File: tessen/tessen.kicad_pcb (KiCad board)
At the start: 2 copper layers, 255.2 x 106.9 mm, 108 parts, among them J1 C, J10 C, J11 C, J12 C, J16 C, J18 C, J19 C, J2 C, J20 C, J21 C, J22 C, J23 C, J24 C, J25 C, J26 C, J27 C, J28 C, J29 C, J3 C, J30 C, J31 C, J32 C, J33 C, J34 C, J4 C, J5 C, J6 C, J7 C, J8 C, J9 C, U1 ProMicro

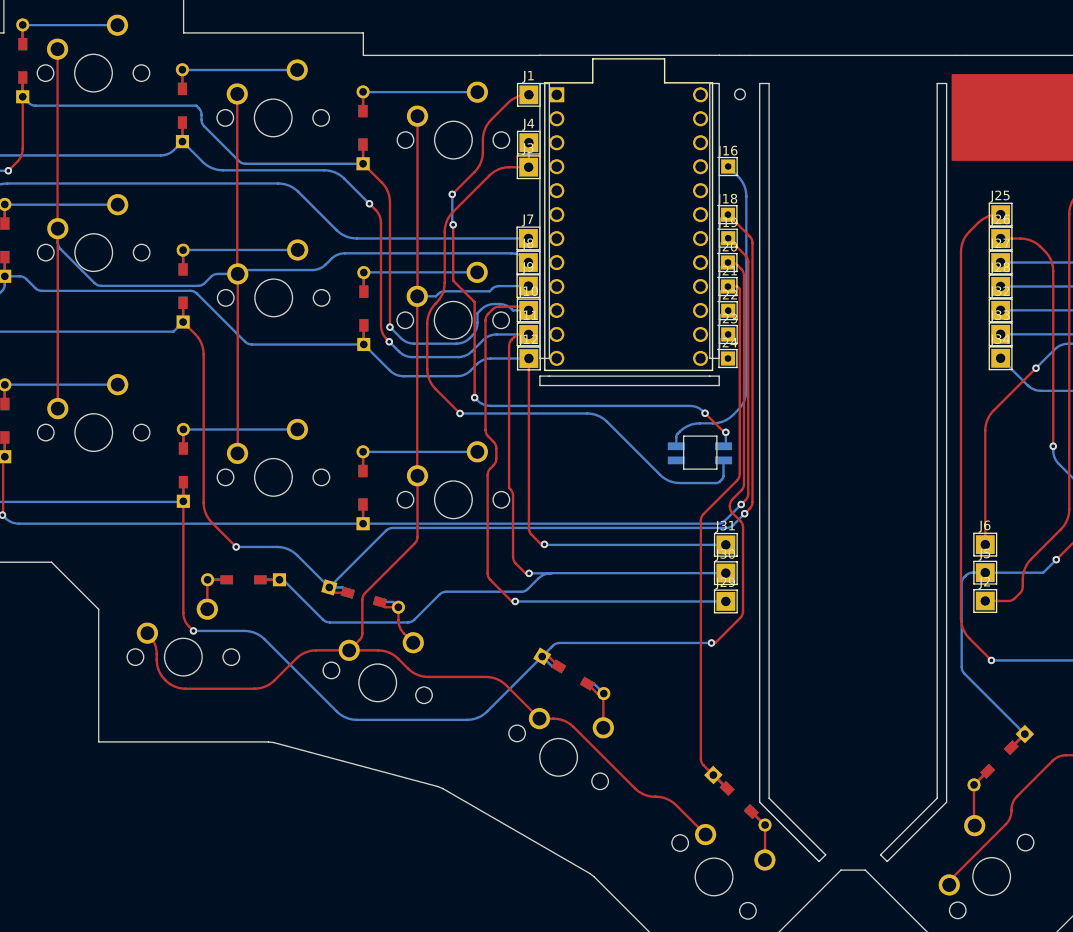
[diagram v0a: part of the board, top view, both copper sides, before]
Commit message: add other kicad projects
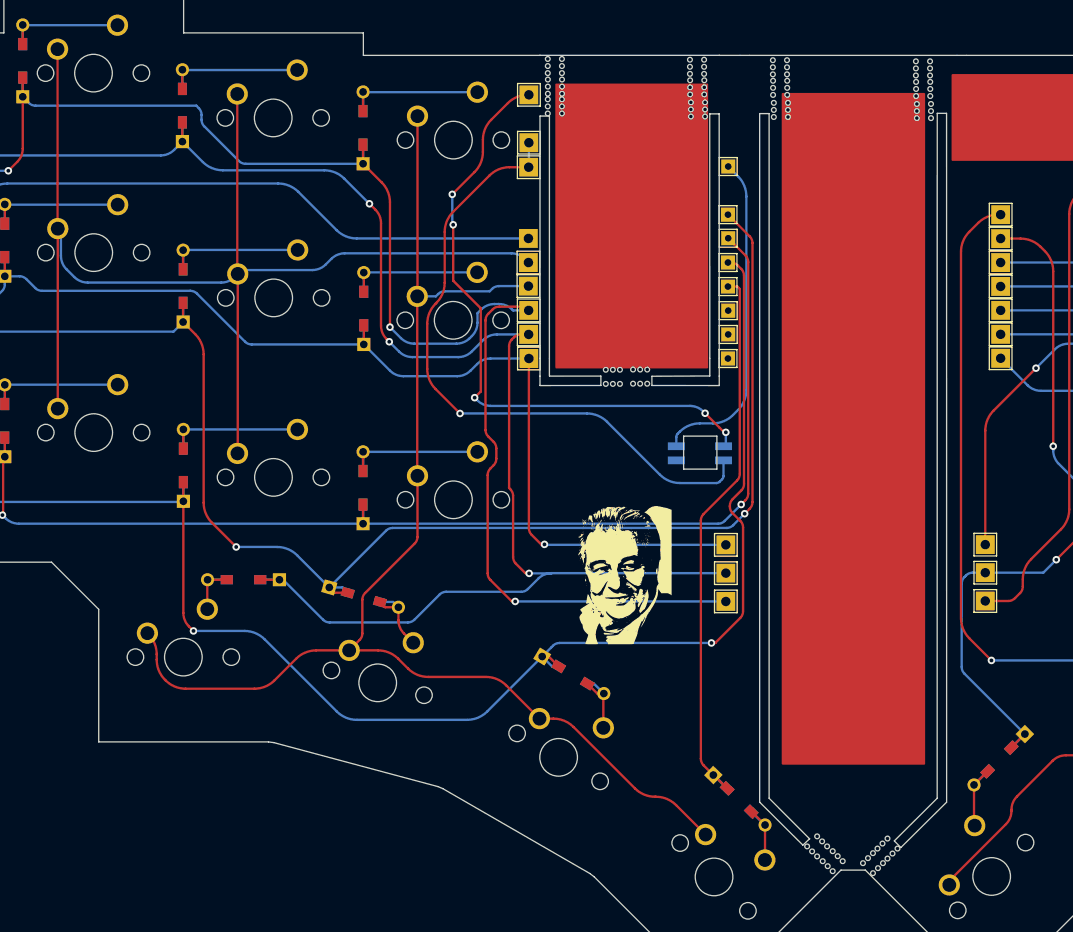
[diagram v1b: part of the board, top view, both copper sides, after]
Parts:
- removed U1: ProMicro, promicro:ProMicro
- added ?: , , F.Cu at (128.3, 60.7)
- added G***: LOGO, cc:cc, F.Cu at (120.6, 110.8)
- added mouse-bite-2mm-slot: VAL**, Panelization:mouse-bite-2mm-slot, F.Cu at (120.0, 90.0)
- added mouse-bite-2mm-slot: VAL**, Panelization:mouse-bite-2mm-slot, F.Cu at (153.0, 61.8)
- added mouse-bite-2mm-slot: VAL**, Panelization:mouse-bite-2mm-slot, F.Cu at (141.6, 139.8)
- added mouse-bite-2mm-slot: VAL**, Panelization:mouse-bite-2mm-slot, F.Cu at (129.0, 61.6)
- added mouse-bite-2mm-slot: VAL**, Panelization:mouse-bite-2mm-slot, F.Cu at (152.9, 57.3)
- added mouse-bite-2mm-slot: VAL**, Panelization:mouse-bite-2mm-slot, F.Cu at (113.8, 61.3)
- added mouse-bite-2mm-slot: VAL**, Panelization:mouse-bite-2mm-slot, F.Cu at (147.6, 141.5)
- added mouse-bite-2mm-slot: VAL**, Panelization:mouse-bite-2mm-slot, F.Cu at (113.8, 57.0)
- added mouse-bite-2mm-slot: VAL**, Panelization:mouse-bite-2mm-slot, F.Cu at (149.1, 140.0)
- added mouse-bite-2mm-slot: VAL**, Panelization:mouse-bite-2mm-slot, F.Cu at (137.7, 57.2)
- added mouse-bite-2mm-slot: VAL**, Panelization:mouse-bite-2mm-slot, F.Cu at (128.9, 57.1)
- added mouse-bite-2mm-slot: VAL**, Panelization:mouse-bite-2mm-slot, F.Cu at (143.3, 141.3)
- added mouse-bite-2mm-slot: VAL**, Panelization:mouse-bite-2mm-slot, F.Cu at (137.8, 61.7)
- added mouse-bite-2mm-slot: VAL**, Panelization:mouse-bite-2mm-slot, F.Cu at (122.9, 90.0)
- added mouse-bite-2mm-slot: VAL**, Panelization:mouse-bite-2mm-slot, F.Cu at (128.9, 59.3)
- added mouse-bite-2mm-slot: VAL**, Panelization:mouse-bite-2mm-slot, F.Cu at (137.7, 59.4)
- added mouse-bite-2mm-slot: VAL**, Panelization:mouse-bite-2mm-slot, F.Cu at (152.9, 59.5)
- added mouse-bite-2mm-slot: VAL**, Panelization:mouse-bite-2mm-slot, F.Cu at (113.9, 59.2)
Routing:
- net LED: track 66.3 -> 66.9 mm
- net COL1: track 131.1 -> 131.6 mm
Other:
- outline, holes or cut-outs redrawn
- board text added: "<- TX for ref (top right pin)"
- board text added: "<- this one isn't connected to the other side"
- board text added: "<--------->"
- board text added: "Connect all of those"
- board text added: "Connect each pro-micro pin to adjacent one if available. You can use diode legs. USB SIDE UP"
